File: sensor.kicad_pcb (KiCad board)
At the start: 2 copper layers, 62 x 65 mm, 92 parts, among them CON1 Micro USB, CON2 PROG, CON3 Jack-DC, CON4 HTU21D, CON5 Conn_01x08, Q1 BSS214N, Q2 BSS214N, Q3 BSS214N, Q4 BSS214N, Q5 BSS214N, Q6 BSS214N, SW1 RESET, SW2 CFG, U1 LM7805, U2 TLV1117LV33DCY, U3 ESP-12F, U4 HTU21D, U5 PMS7003

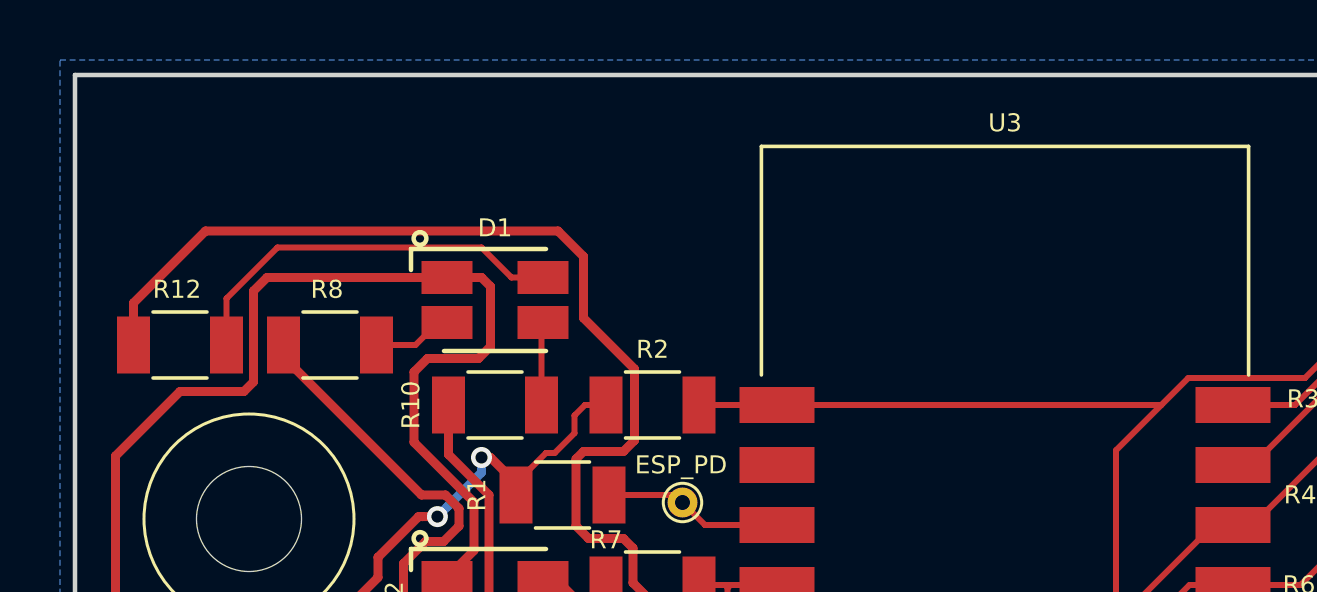
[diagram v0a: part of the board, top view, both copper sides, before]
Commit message: Added licensing information, Open Hardware logo, project URL, etc.
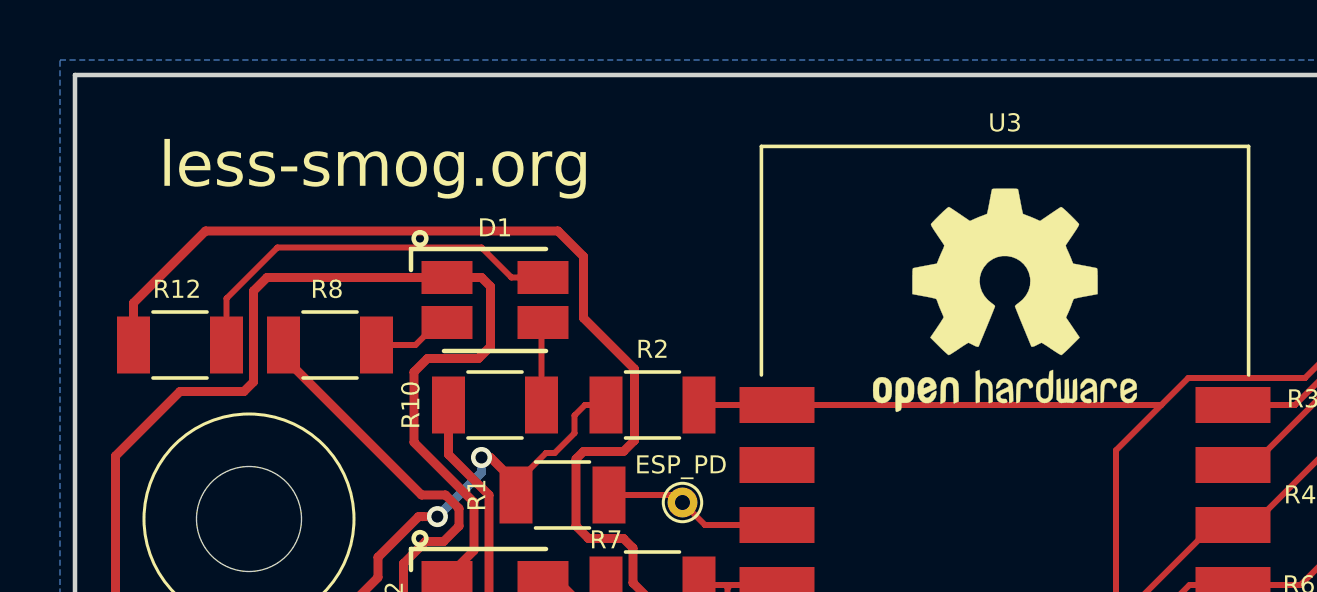
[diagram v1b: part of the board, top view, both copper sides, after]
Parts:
- added REF***: OSHW-Logo2_9.8x8mm_SilkScreen, Symbols:OSHW-Logo2_9.8x8mm_SilkScreen, F.Cu at (97.0, 49.0)
- added REF***: KiCad-Logo2_6mm_SilkScreen, Symbols:KiCad-Logo2_6mm_SilkScreen, B.Cu at (124.0, 66.5)
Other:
- board text added: "Licensed under CERN Open Hardware License 1.2 Revision 1"
- board text added: "PMS3003/5003"
- board text added: "PMS7003"
- board text added: "less-smog.org"

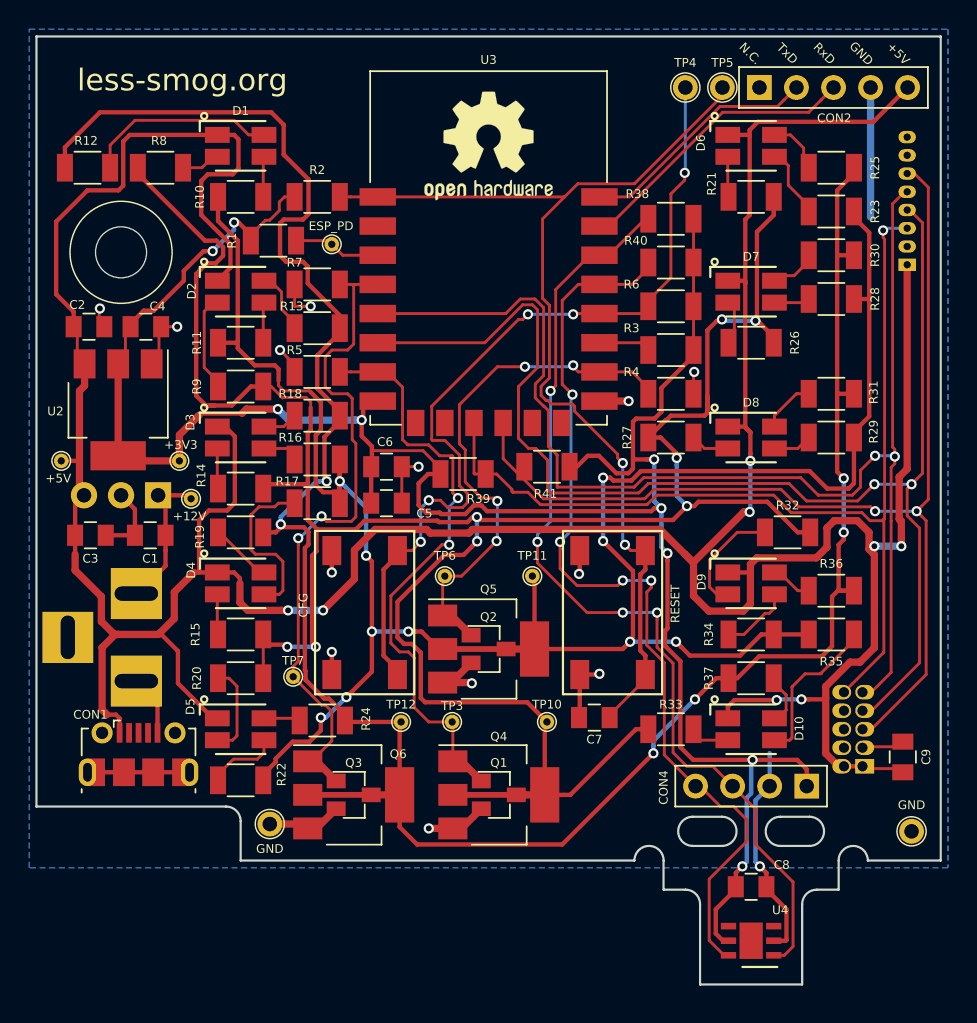
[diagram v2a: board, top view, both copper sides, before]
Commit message: Update PCB to for production: - change via drills to 0.3mm - update solder mask expansion - update paste mask expansion - generate gerber files
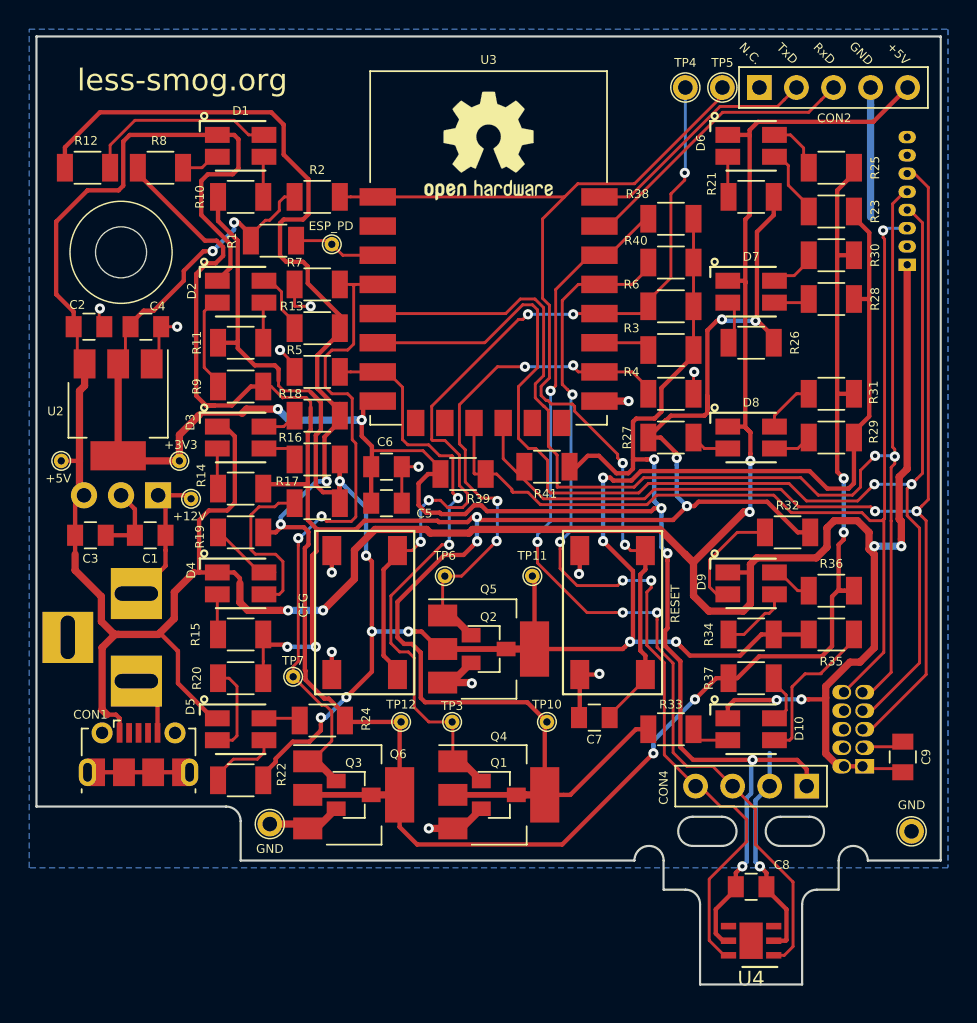
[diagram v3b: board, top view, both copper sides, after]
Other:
- net class Default: via_drill 0.4 -> 0.3
- net class Power: via_drill 0.4 -> 0.3
- rule pad_to_mask_clearance: 0.2 -> 0.1
- rule via_min_drill: 0.4 -> 0.3
